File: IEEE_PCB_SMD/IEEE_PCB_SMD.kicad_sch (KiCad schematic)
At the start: 17 parts, among them U1 555, U2 4017, U3 EG1218, U5 CR2025TR

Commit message: Rev 10/8/22
changed the logo footprint
changed the resistor footprint
added more vias to the power
altered traces to better fit the ESR standards
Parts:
- R1: footprint Resistor_THT:R_Axial_DIN0309_L9.0mm_D3.2mm_P12.70mm_Horizontal -> Resistor_THT:R_Axial_DIN0207_L6.3mm_D2.5mm_P7.62mm_Horizontal
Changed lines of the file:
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@@
       (effects (font (size 1.27 1.27)) (justify left))
     )
-    (property "Footprint" "Resistor_THT:R_Axial_DIN0309_L9.0mm_D3.2mm_P12.70mm_Horizontal" (id 2) (at 251.46 43.18 0)
+    (property "Footprint" "Resistor_THT:R_Axial_DIN0207_L6.3mm_D2.5mm_P7.62mm_Horizontal" (id 2) (at 251.46 43.18 0)
       (effects (font (size 1.27 1.27)) hide)
     )
@@
   (symbol (lib_id "IEEE_PCB_SMD-rescue:+3.3V-power") (at 224.79 111.76 0) (unit 1)
     (in_bom yes) (on_board yes)
-    (property "Reference" "#PWR?" (id 0) (at 224.79 115.57 0)
+    (property "Reference" "#PWR0107" (id 0) (at 224.79 115.57 0)
       (effects (font (size 1.27 1.27)) hide)
     )
@@
       (reference "#PWR0106") (unit 1) (value "GND") (footprint "")
     )
+    (path "/c30cd767-325c-4d2b-a5ac-695b260f4bf4"
+      (reference "#PWR0107") (unit 1) (value "+3.3V") (footprint "")
+    )
     (path "/00000000-0000-0000-0000-000063187633"
       (reference "#PWR0108") (unit 1) (value "GND") (footprint "")
@@
       (reference "#PWR0110") (unit 1) (value "+3.3V") (footprint "")
     )
-    (path "/c30cd767-325c-4d2b-a5ac-695b260f4bf4"
-      (reference "#PWR?") (unit 1) (value "+3.3V") (footprint "")
-    )
     (path "/00000000-0000-0000-0000-000062f9d4fb"
       (reference "C1") (unit 1) (value "0.01 uF") (footprint "Capacitor_THT:CP_Radial_D5.0mm_P2.00mm")
@@
     )
     (path "/00000000-0000-0000-0000-000062fa117c"
-      (reference "R1") (unit 1) (value "1k") (footprint "Resistor_THT:R_Axial_DIN0309_L9.0mm_D3.2mm_P12.70mm_Horizontal")
+      (reference "R1") (unit 1) (value "1k") (footprint "Resistor_THT:R_Axial_DIN0207_L6.3mm_D2.5mm_P7.62mm_Horizontal")
     )
     (path "/00000000-0000-0000-0000-000062f9fcbf"

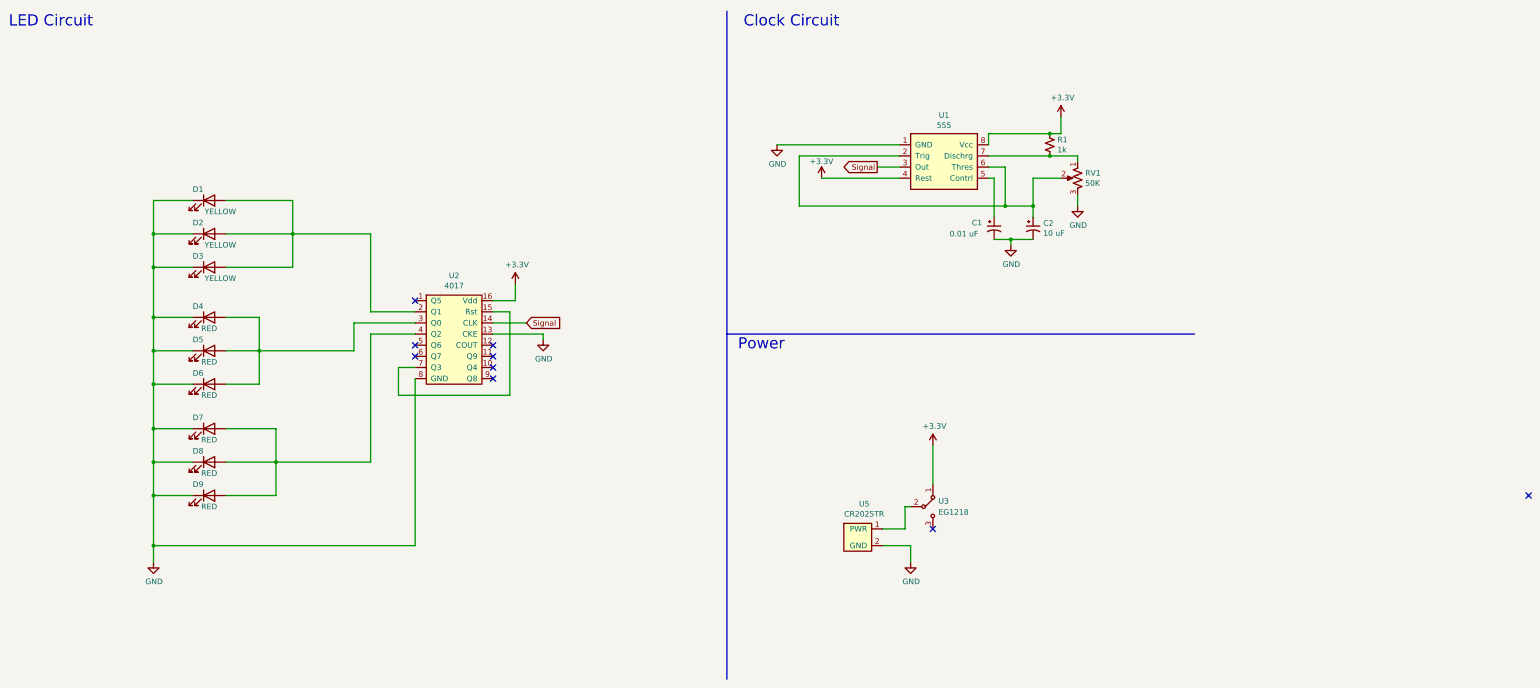
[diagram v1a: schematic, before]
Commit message: Rev - Matthew
Snowflake changes:
Fixed battery and switch symbols
added 100 ohm resistors 603
looked at traces - not acid traps that I see

will work on the ball soon
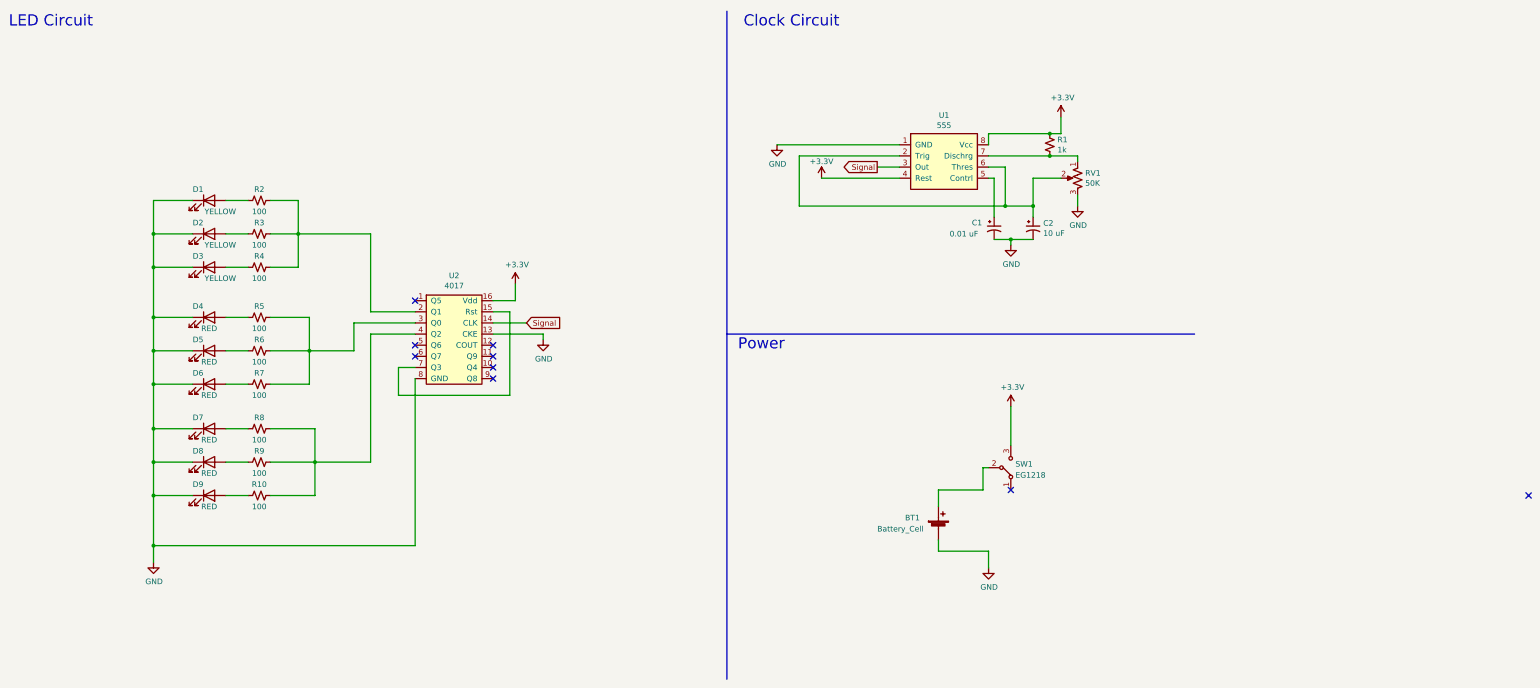
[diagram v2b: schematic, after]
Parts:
- removed U3: EG1218, IEEE_Ornament:EG1218, symbol IEEE_PCB_SMD-rescue:EG1218-IEEE_PCB_Ornament
- removed U5: CR2025TR, IEEE_Ornament:CR2025TR, symbol IEEE_PCB_SMD-rescue:CR2025TR-IEEE_PCB_Ornament
- added BT1: Battery_Cell, IEEE_Ornament:CR2025TR, symbol Device:Battery_Cell
- added R10, R2, R3, R4, R5, R6, R7, R8, R9: 100, Resistor_SMD:R_0603_1608Metric_Pad0.98x0.95mm_HandSolder, symbol Device:R_Small_US
- added SW1: EG1218, IEEE_Ornament:EG1218, symbol IEEE_Ornament:EG1218
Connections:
- net +3V3: now also SW1.3
- net GND: now also BT1.2 (-)
- new net: R2.1, R3.1, R4.1, U2.2 (Q1)
- new net: R5.1, R6.1, R7.1, U2.3 (Q0)
- new net: R10.1, R8.1, R9.1, U2.4 (Q2)
- new net: D1.2 (A), R2.2
- new net: D2.2 (A), R3.2
- new net: D3.2 (A), R4.2
- new net: D4.2 (A), R5.2
- new net: D5.2 (A), R6.2
- new net: D6.2 (A), R7.2
- new net: D7.2 (A), R8.2
- new net: D8.2 (A), R9.2
- new net: D9.2 (A), R10.2
- new net: BT1.1 (+), SW1.2

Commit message: Demo(Test)
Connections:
- net GND: no longer RV1.3
- no-connect marks 9 -> 10
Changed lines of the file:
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@@
   (junction (at 46.99 90.17) (diameter 0) (color 0 0 0 0)
   )
+  (no_connect (at 257.81 54.61))
   (no_connect (at 106.68 88.9))
   (no_connect (at 360.68 123.19))
@@
     (stroke (width 0) (type default) (color 0 0 0 0))
   )
-  (wire (pts (xy 257.81 54.61) (xy 257.81 57.15))
-    (stroke (width 0) (type default) (color 0 0 0 0))
-  )
   (wire (pts (xy 82.55 90.17) (xy 92.71 90.17))
     (stroke (width 0) (type default) (color 0 0 0 0))
@@
     (pin "1")
   )
-  (symbol (lib_id "power:GND") (at 257.81 57.15 0) (unit 1)
-    (in_bom yes) (on_board yes)
-    (property "Reference" "#PWR0103" (id 0) (at 257.81 63.5 0)
-      (effects (font (size 1.27 1.27)) hide)
-    )
-    (property "Value" "GND" (id 1) (at 257.937 61.5442 0))
-    (property "Footprint" "" (id 2) (at 257.81 57.15 0)
-      (effects (font (size 1.27 1.27)) hide)
-    )
-    (property "Datasheet" "" (id 3) (at 257.81 57.15 0)
-      (effects (font (size 1.27 1.27)) hide)
-    )
-    (pin "1")
-  )
   (symbol (lib_id "power:GND") (at 189.23 43.18 0) (unit 1)
     (in_bom yes) (on_board yes)
@@
       (reference "#PWR0102") (unit 1) (value "+3.3V") (footprint "")
     )
-    (path "/00000000-0000-0000-0000-000062fa648c"
-      (reference "#PWR0103") (unit 1) (value "GND") (footprint "")
-    )
     (path "/00000000-0000-0000-0000-000062fa6c11"
